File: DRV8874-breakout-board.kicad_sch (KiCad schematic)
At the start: 16 parts, among them J102 Conn_01x02_Pin, J104 Conn_01x06_Pin, J105 PMODE, J305 M0_CONN

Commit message: Additional changes
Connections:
- net +3V3: now also J104.4 (Pin_4); no longer J104.1 (Pin_1)
- net GND: now also J104.5 (Pin_5); no longer J104.2 (Pin_2)
- net IPROPI: now also J104.3 (Pin_3); no longer J104.5 (Pin_5)
- net nFAULT: now also J104.2 (Pin_2); no longer J104.4 (Pin_4)
- net nSLEEP: now also J104.1 (Pin_1); no longer J104.3 (Pin_3)
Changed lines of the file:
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@@
-    (stroke (width 0) (type default))
-  )
-  (wire (pts (xy 71.12 91.44) (xy 83.82 91.44))
     (stroke (width 0) (type default))
   )
@@
     (stroke (width 0) (type default))
   )
+  (wire (pts (xy 71.12 96.52) (xy 82.55 96.52))
+    (stroke (width 0) (type default))
+  )
   (wire (pts (xy 154.94 87.63) (xy 158.75 87.63))
     (stroke (width 0) (type default))
@@
     (stroke (width 0) (type default))
   )
-  (wire (pts (xy 71.12 88.9) (xy 83.82 88.9))
-    (stroke (width 0) (type default))
-  )
   (wire (pts (xy 170.18 105.41) (xy 170.18 113.03))
     (stroke (width 0) (type default))
   )
   (wire (pts (xy 158.75 81.28) (xy 176.53 81.28))
+    (stroke (width 0) (type default))
+  )
+  (wire (pts (xy 71.12 99.06) (xy 82.55 99.06))
     (stroke (width 0) (type default))
   )
@@
     )
   )
-  (global_label "nFAULT" (shape input) (at 71.12 96.52 0)
+  (global_label "nFAULT" (shape input) (at 71.12 91.44 0)
     (effects (font (size 1.27 1.27)) (justify left))
-    (property "Intersheetrefs" "${INTERSHEET_REFS}" (at 71.12 96.52 0)
+    (property "Intersheetrefs" "${INTERSHEET_REFS}" (at 71.12 91.44 0)
       (effects (font (size 1.27 1.27)) hide)
     )
@@
     )
   )
-  (global_label "IPROPI" (shape input) (at 71.12 99.06 0)
+  (global_label "IPROPI" (shape input) (at 71.12 93.98 0)
     (effects (font (size 1.27 1.27)) (justify left))
-    (property "Intersheetrefs" "${INTERSHEET_REFS}" (at 71.12 99.06 0)
+    (property "Intersheetrefs" "${INTERSHEET_REFS}" (at 71.12 93.98 0)
       (effects (font (size 1.27 1.27)) hide)
     )
@@
     )
   )
-  (global_label "nSLEEP" (shape input) (at 71.12 93.98 0)
+  (global_label "nSLEEP" (shape input) (at 71.12 88.9 0)
     (effects (font (size 1.27 1.27)) (justify left))
-    (property "Intersheetrefs" "${INTERSHEET_REFS}" (at 71.12 93.98 0)
+    (property "Intersheetrefs" "${INTERSHEET_REFS}" (at 71.12 88.9 0)
       (effects (font (size 1.27 1.27)) hide)
     )
@@
     )
   )
-  (symbol (lib_id "power:GND") (at 83.82 91.44 0) (unit 1)
-    (in_bom yes) (on_board yes) (dnp no)
-    (property "Reference" "#PWR0323" (at 83.82 97.79 0)
-      (effects (font (size 1.27 1.27)) hide)
-    )
-    (property "Value" "GND" (at 83.947 95.8342 0)
-      (effects (font (size 1.27 1.27)))
-    )
-    (property "Footprint" "" (at 83.82 91.44 0)
-      (effects (font (size 1.27 1.27)) hide)
-    )
-    (property "Datasheet" "" (at 83.82 91.44 0)
+  (symbol (lib_id "power:GND") (at 82.55 99.06 0) (unit 1)
+    (in_bom yes) (on_board yes) (dnp no)
+    (property "Reference" "#PWR0323" (at 82.55 105.41 0)
+      (effects (font (size 1.27 1.27)) hide)
+    )
+    (property "Value" "GND" (at 82.677 103.4542 0)
+      (effects (font (size 1.27 1.27)))
+    )
+    (property "Footprint" "" (at 82.55 99.06 0)
+      (effects (font (size 1.27 1.27)) hide)
+    )
+    (property "Datasheet" "" (at 82.55 99.06 0)
       (effects (font (size 1.27 1.27)) hide)
     )
@@
     )
   )
-  (symbol (lib_id "smart_motor_controller-rescue:+3.3V-power") (at 83.82 88.9 0) (unit 1)
-    (in_bom yes) (on_board yes) (dnp no)
-    (property "Reference" "#PWR0324" (at 83.82 92.71 0)
-      (effects (font (size 1.27 1.27)) hide)
-    )
-    (property "Value" "+3.3V" (at 80.01 87.63 0)
-      (effects (font (size 1.27 1.27)))
-    )
-    (property "Footprint" "" (at 83.82 88.9 0)
-      (effects (font (size 1.27 1.27)) hide)
-    )
-    (property "Datasheet" "" (at 83.82 88.9 0)
-      (effects (font (size 1.27 1.27)) hide)
-    )
+  (symbol (lib_id "smart_motor_controller-rescue:+3.3V-power") (at 82.55 96.52 0) (unit 1)
+    (in_bom yes) (on_board yes) (dnp no)
+    (property "Reference" "#PWR0324" (at 82.55 100.33 0)
+      (effects (font (size 1.27 1.27)) hide)
+    )
+    (property "Value" "+3.3V" (at 78.74 95.25 0)
+      (effects (font (size 1.27 1.27)))
+    )
+    (property "Footprint" "" (at 82.55 96.52 0)
+      (effects (font (size 1.27 1.27)) hide)
+    )
+    (property "Datasheet" "" (at 82.55 96.52 0)
+      (effects (font (size 1.27 1.27)) hide)
+    )

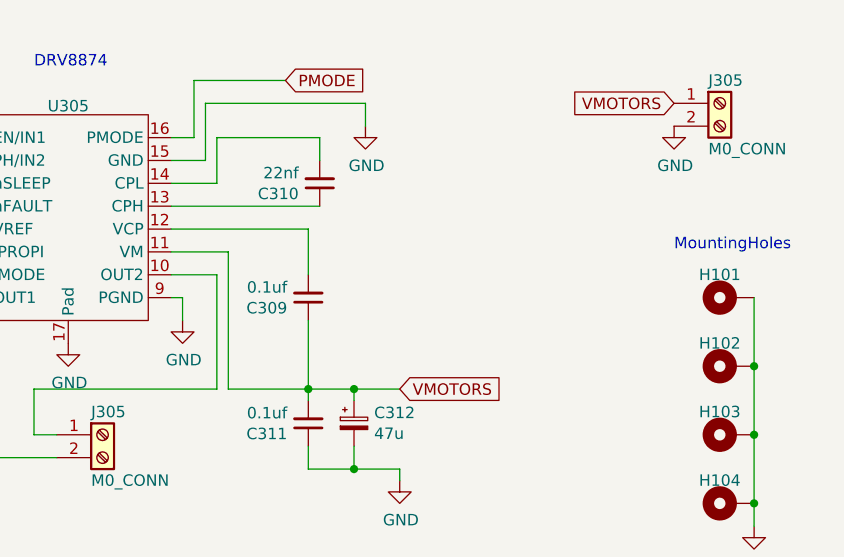
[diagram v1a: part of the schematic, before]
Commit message: First release version
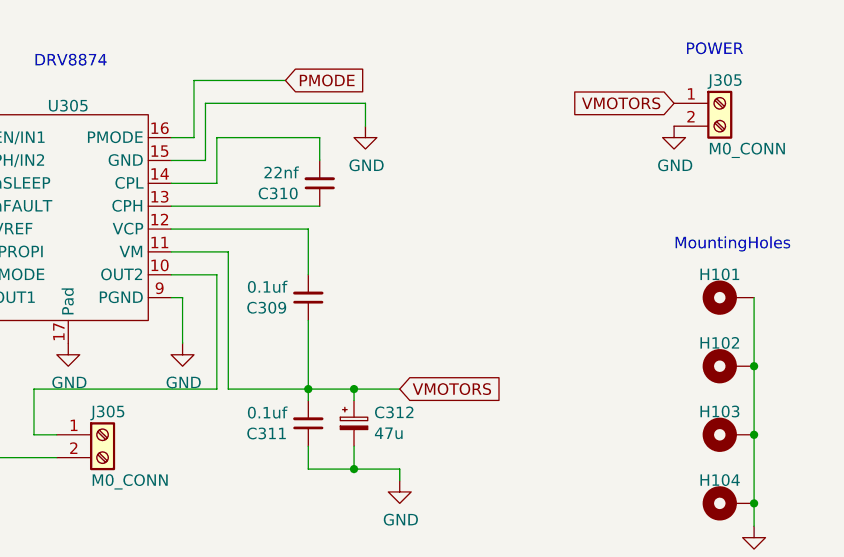
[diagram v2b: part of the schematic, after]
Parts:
- J305: LCSC Part # In stock -> C8269
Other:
- note added: "POWER"
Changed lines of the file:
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@@
     (stroke (width 0) (type default))
   )
-  (wire (pts (xy 156.21 102.87) (xy 156.21 105.41))
+  (wire (pts (xy 156.21 102.87) (xy 156.21 107.95))
     (stroke (width 0) (type default))
   )
@@
   )
   (text "MountingHoles" (at 210.82 97.79 0)
+    (effects (font (size 1.27 1.27)) (justify left bottom))
+  )
+  (text "POWER" (at 212.09 76.2 0)
     (effects (font (size 1.27 1.27)) (justify left bottom))
   )
@@
     )
   )
-  (symbol (lib_id "power:GND") (at 156.21 105.41 0) (unit 1)
-    (in_bom yes) (on_board yes) (dnp no)
-    (property "Reference" "#PWR0317" (at 156.21 111.76 0)
-      (effects (font (size 1.27 1.27)) hide)
-    )
-    (property "Value" "GND" (at 156.337 109.8042 0)
-      (effects (font (size 1.27 1.27)))
-    )
-    (property "Footprint" "" (at 156.21 105.41 0)
-      (effects (font (size 1.27 1.27)) hide)
-    )
-    (property "Datasheet" "" (at 156.21 105.41 0)
+  (symbol (lib_id "power:GND") (at 156.21 107.95 0) (unit 1)
+    (in_bom yes) (on_board yes) (dnp no)
+    (property "Reference" "#PWR0317" (at 156.21 114.3 0)
+      (effects (font (size 1.27 1.27)) hide)
+    )
+    (property "Value" "GND" (at 156.337 112.3442 0)
+      (effects (font (size 1.27 1.27)))
+    )
+    (property "Footprint" "" (at 156.21 107.95 0)
+      (effects (font (size 1.27 1.27)) hide)
+    )
+    (property "Datasheet" "" (at 156.21 107.95 0)
       (effects (font (size 1.27 1.27)) hide)
     )
@@
       (effects (font (size 1.27 1.27)) hide)
     )
-    (property "LCSC Part #" "In stock" (at 215.9 81.28 0)
+    (property "LCSC Part #" "C8269" (at 215.9 81.28 0)
       (effects (font (size 1.27 1.27)) hide)
     )
@@
       (effects (font (size 1.27 1.27)) hide)
     )
-    (property "LCSC Part #" "In stock" (at 147.32 118.11 0)
-      (effects (font (size 1.27 1.27)) hide)
-    )
+    (property "LCSC Part #" "C8269" (at 147.32 118.11 0)
+      (effects (font (size 1.27 1.27)) hide)
+    )

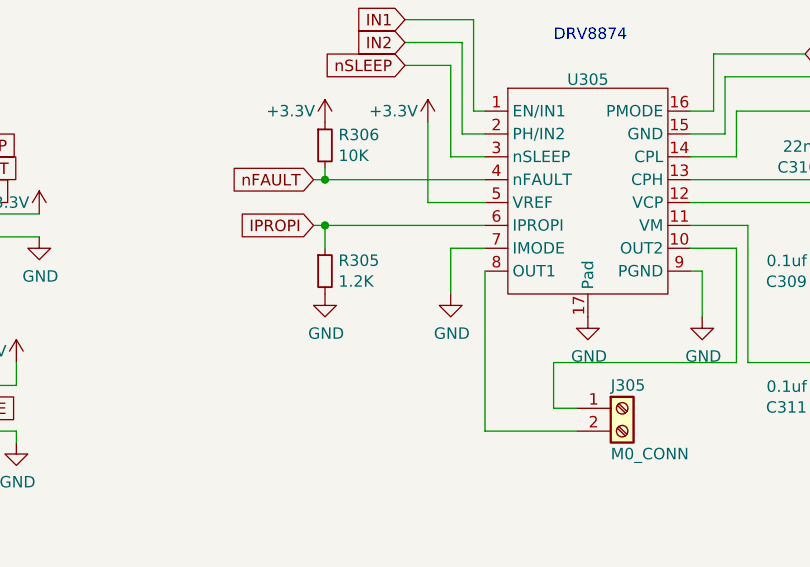
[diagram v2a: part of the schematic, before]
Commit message: Added external resistor
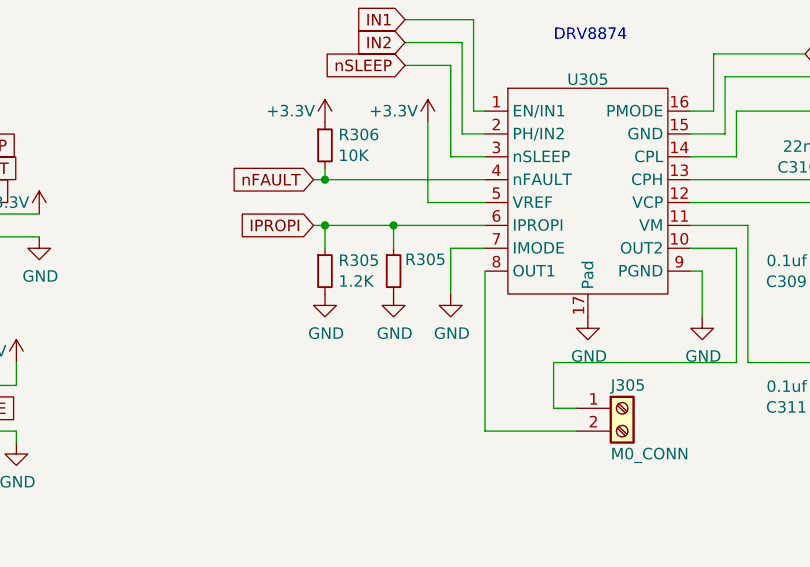
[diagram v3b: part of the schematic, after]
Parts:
- added R305: ~, Resistor_THT:R_Axial_DIN0204_L3.6mm_D1.6mm_P5.08mm_Horizontal, symbol Device:R_Small
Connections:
- net GND: now also R305.2
- net IPROPI: now also R305.1
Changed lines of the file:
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@@
   (junction (at 170.18 113.03) (diameter 0) (color 0 0 0 0)
   )
+  (junction (at 121.92 97.79) (diameter 0) (color 0 0 0 0)
+  )
   (junction (at 219.71 125.73) (diameter 0) (color 0 0 0 0)
   )
@@
     (stroke (width 0) (type default))
   )
+  (wire (pts (xy 121.92 97.79) (xy 132.08 97.79))
+    (stroke (width 0) (type default))
+  )
   (wire (pts (xy 170.18 113.03) (xy 175.26 113.03))
     (stroke (width 0) (type default))
@@
     (stroke (width 0) (type default))
   )
+  (wire (pts (xy 121.92 97.79) (xy 121.92 100.33))
+    (stroke (width 0) (type default))
+  )
   (wire (pts (xy 114.3 92.71) (xy 132.08 92.71))
     (stroke (width 0) (type default))
@@
     (stroke (width 0) (type default))
   )
-  (wire (pts (xy 114.3 97.79) (xy 132.08 97.79))
+  (wire (pts (xy 114.3 97.79) (xy 121.92 97.79))
     (stroke (width 0) (type default))
   )
@@
     )
   )
+  (symbol (lib_id "power:GND") (at 121.92 105.41 0) (unit 1)
+    (in_bom yes) (on_board yes) (dnp no)
+    (property "Reference" "#PWR0322" (at 121.92 111.76 0)
+      (effects (font (size 1.27 1.27)) hide)
+    )
+    (property "Value" "GND" (at 122.047 109.8042 0)
+      (effects (font (size 1.27 1.27)))
+    )
+    (property "Footprint" "" (at 121.92 105.41 0)
+      (effects (font (size 1.27 1.27)) hide)
+    )
+    (property "Datasheet" "" (at 121.92 105.41 0)
+      (effects (font (size 1.27 1.27)) hide)
+    )
+    (pin "1")
+    (instances
+      (project "smart_motor_controller"
+        (path "/54a8299a-8af5-4797-a59a-a6e866f823f7/00000000-0000-0000-0000-000060a3e5c0"
+          (reference "#PWR0322") (unit 1)
+        )
+        (path "/54a8299a-8af5-4797-a59a-a6e866f823f7"
+          (reference "#PWR?") (unit 1)
+        )
+      )
+      (project "DRV8874-breakout-board"
+        (path "/f80f1429-74da-4a85-b374-ac620f483f97"
+          (reference "#PWR0115") (unit 1)
+        )
+      )
+    )
+  )
   (symbol (lib_id "Device:C_Small") (at 170.18 116.84 180) (unit 1)
     (in_bom yes) (on_board yes) (dnp no)
@@
         )
       )
+    )
+  )
+  (symbol (lib_id "Device:R_Small") (at 121.92 102.87 0) (unit 1)
+    (in_bom yes) (on_board yes) (dnp no)
+    (property "Reference" "R305" (at 123.19 101.6 0)
+      (effects (font (size 1.27 1.27)) (justify left))
+    )
+    (property "Value" "~" (at 123.4186 104.013 0)
+      (effects (font (size 1.27 1.27)) (justify left))
+    )
+    (property "Footprint" "Resistor_THT:R_Axial_DIN0204_L3.6mm_D1.6mm_P5.08mm_Horizontal" (at 121.92 102.87 0)
+      (effects (font (size 1.27 1.27)) hide)
+    )
+    (property "Datasheet" "~" (at 121.92 102.87 0)
+      (effects (font (size 1.27 1.27)) hide)
+    )
+    (property "LCSC Part #" "C114605" (at 121.92 102.87 0)
+      (effects (font (size 1.27 1.27)) hide)
+    )
+    (pin "1")
+    (pin "2")
+    (instances
+      (project "smart_motor_controller"
+        (path "/54a8299a-8af5-4797-a59a-a6e866f823f7/00000000-0000-0000-0000-000060a3e5c0"
+          (reference "R305") (unit 1)
+        )
+        (path "/54a8299a-8af5-4797-a59a-a6e866f823f7"
+          (reference "R?") (unit 1)
+        )
+      )
+      (project "DRV8874-breakout-board"
+        (path "/f80f1429-74da-4a85-b374-ac620f483f97"
+          (reference "R103") (unit 1)
+        )
+      )

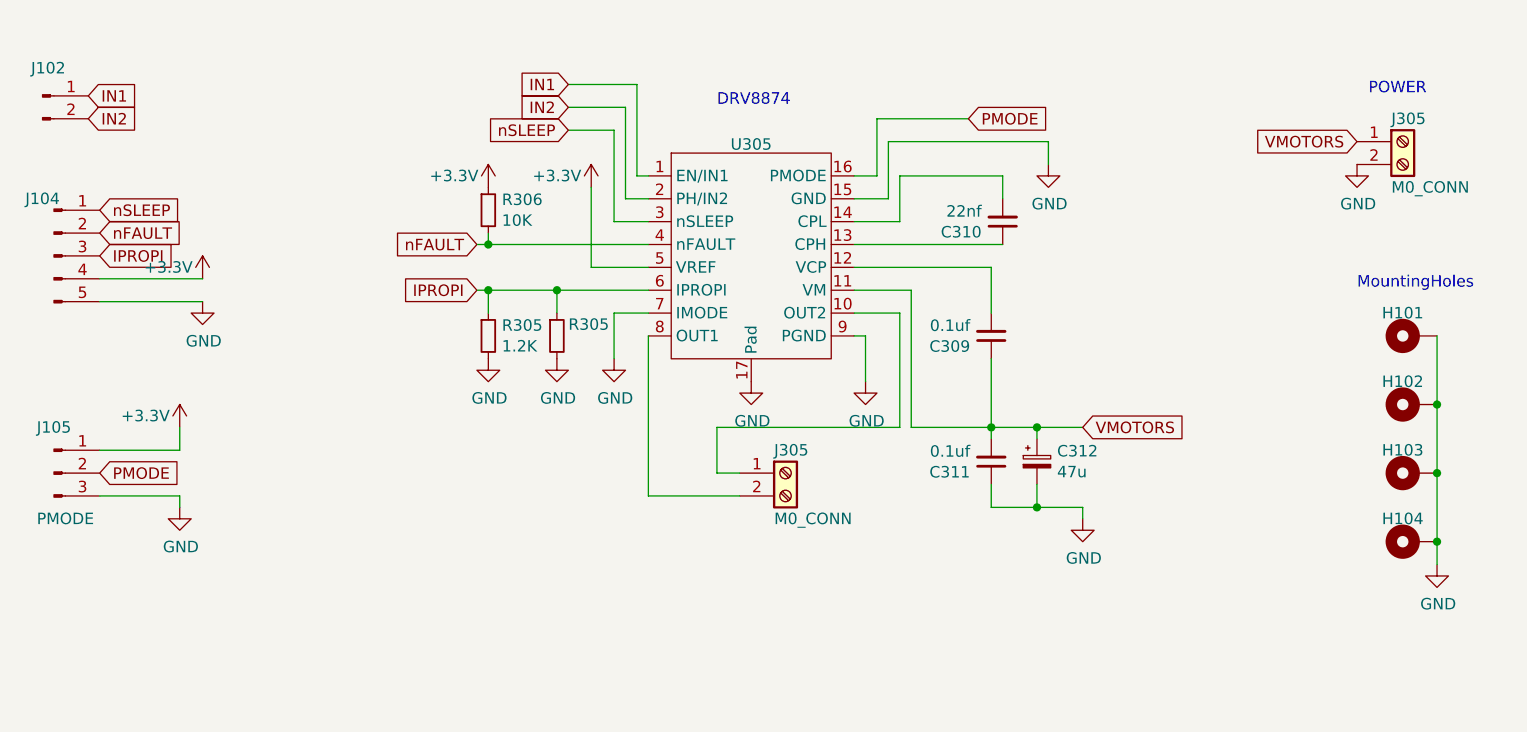
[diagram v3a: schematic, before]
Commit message: Added trace zones
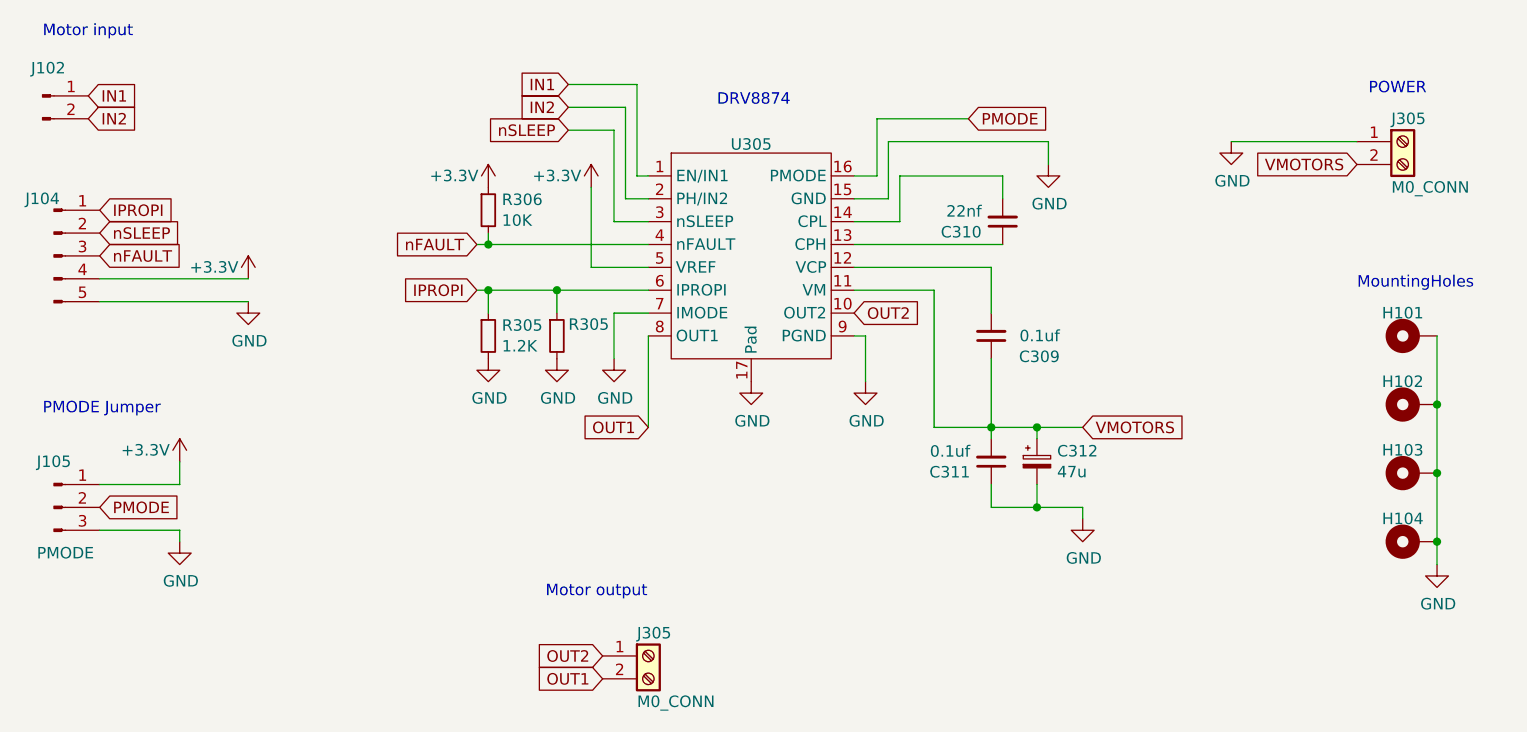
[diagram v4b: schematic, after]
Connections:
- net GND: now also J305.1 (Pin_1); no longer J305.2 (Pin_2)
- net IPROPI: now also J104.1 (Pin_1); no longer J104.3 (Pin_3)
- net VMOTORS: now also J305.2 (Pin_2); no longer J305.1 (Pin_1)
- net nFAULT: now also J104.3 (Pin_3); no longer J104.2 (Pin_2)
- net nSLEEP: now also J104.2 (Pin_2); no longer J104.1 (Pin_1)
- net OUT2: now reaches J305.1 (Pin_1), U305.10 (OUT2)
- net OUT1: now reaches J305.2 (Pin_2), U305.8 (OUT1)
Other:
- note added: "Motor input"
- note added: "Motor output"
- note added: "PMODE Jumper"
- moved on the sheet: J105, J305

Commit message: Update screw terminal
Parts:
- J305: footprint VsReality_Footprints:Ningbo_Kangnex_Elec_WJ128V_5_0_2P -> VsReality_Footprints:JILN JL126-50002G01; LCSC Part # C8269 -> C394556
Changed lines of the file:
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@@
       (effects (font (size 1.27 1.27)) (justify left))
     )
-    (property "Footprint" "VsReality_Footprints:Ningbo_Kangnex_Elec_WJ128V_5_0_2P" (at 215.9 81.28 0)
+    (property "Footprint" "VsReality_Footprints:JILN JL126-50002G01" (at 215.9 81.28 0)
       (effects (font (size 1.27 1.27)) hide)
     )
@@
       (effects (font (size 1.27 1.27)) hide)
     )
-    (property "LCSC Part #" "C8269" (at 215.9 81.28 0)
+    (property "LCSC Part #" "C394556" (at 215.9 81.28 0)
       (effects (font (size 1.27 1.27)) hide)
     )
@@
       (effects (font (size 1.27 1.27)) (justify left))
     )
-    (property "Footprint" "VsReality_Footprints:Ningbo_Kangnex_Elec_WJ128V_5_0_2P" (at 132.08 138.43 0)
+    (property "Footprint" "VsReality_Footprints:JILN JL126-50002G01" (at 132.08 138.43 0)
       (effects (font (size 1.27 1.27)) hide)
     )
@@
       (effects (font (size 1.27 1.27)) hide)
     )
-    (property "LCSC Part #" "C8269" (at 132.08 138.43 0)
+    (property "LCSC Part #" "C394556" (at 132.08 138.43 0)
       (effects (font (size 1.27 1.27)) hide)
     )
